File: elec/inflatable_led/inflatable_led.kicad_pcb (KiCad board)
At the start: 2 copper layers, 100.1 x 100 mm, 87 parts, among them J1 Header-Male-2.54_1x20, J2 Conn_01x02_Pin, J3 Conn_01x02_Pin, SW1 TS-1093C-A7B2-D1, U1 RP2040, U2 W25Q128JVSIQTR, U3 TPS61165DRVR, U4 BQ24040DSQR, U5 AMS1117-3.3, U6 F.0603.00026/P2-0603B1TS2-06T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, U7 SI2323DS, X1 X322512MSB4SI

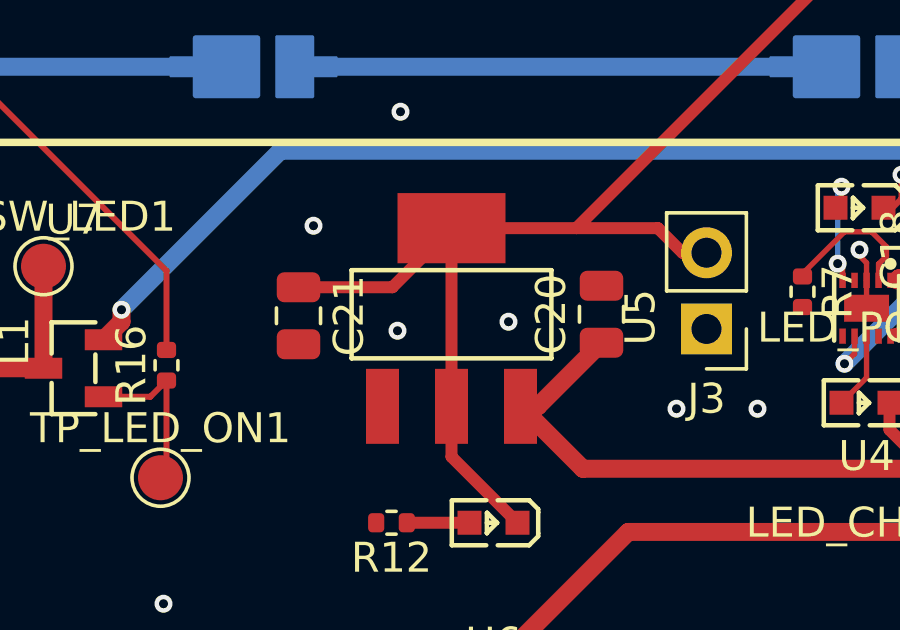
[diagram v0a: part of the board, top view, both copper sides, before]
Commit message: fix footprint + add pn
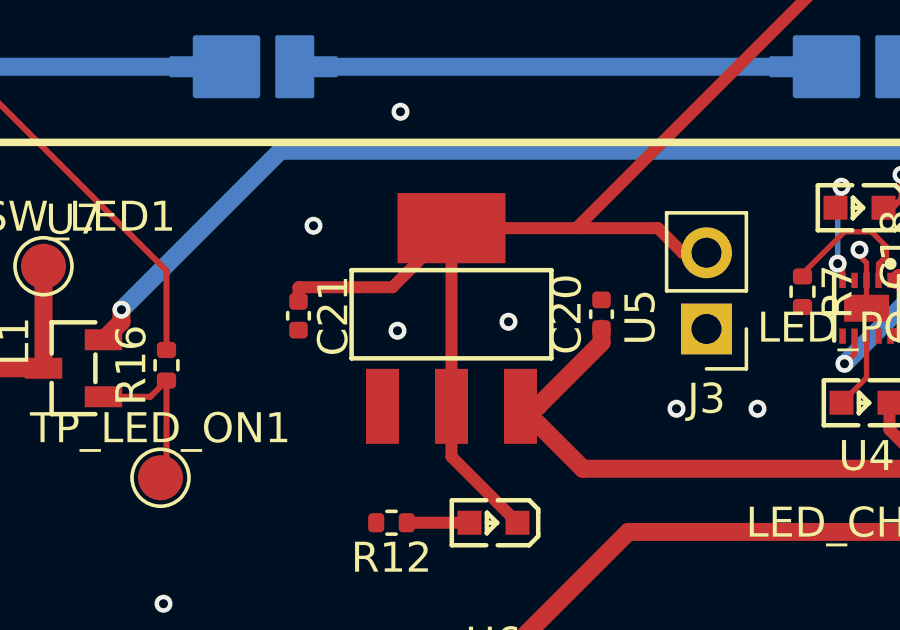
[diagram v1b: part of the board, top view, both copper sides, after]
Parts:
- C20, C21: footprint Capacitor_SMD:C_0805_2012Metric -> Capacitor_SMD:C_0402_1005Metric
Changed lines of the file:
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@@
 		)
 	)
-	(footprint "Capacitor_SMD:C_0805_2012Metric"
+	(footprint "Capacitor_SMD:C_0402_1005Metric"
 		(layer "F.Cu")
 		(at 111.6 128.25 90)
-		(descr "Capacitor SMD 0805 (2012 Metric), square (rectangular) end terminal, IPC_7351 nominal, (Body size source: IPC-SM-782 page 76, https://www.pcb-3d.com/wordpress/wp-content/uploads/ipc-sm-782a_amendment_1_and_2.pdf, https://docs.google.com/spreadsheets/d/1BsfQQcO9C6DZCsRaXUlFlo91Tg2WpOkGARC1WS5S8t0/edit?usp=sharing), generated with kicad-footprint-generator")
+		(descr "Capacitor SMD 0402 (1005 Metric), square (rectangular) end terminal, IPC_7351 nominal, (Body size source: IPC-SM-782 page 76, https://www.pcb-3d.com/wordpress/wp-content/uploads/ipc-sm-782a_amendment_1_and_2.pdf), generated with kicad-footprint-generator")
 		(tags "capacitor")
 		(property "Reference" "C20"
-			(at 0 -1.68 -90)
+			(at 0 -1.16 90)
 			(layer "F.SilkS")
 			(effects
@@
 		)
 		(property "Value" "100nF"
-			(at 0 1.68 -90)
+			(at 0 1.16 90)
 			(layer "F.Fab")
 			(effects
@@
 			)
 		)
-		(property "Footprint" "Capacitor_SMD:C_0805_2012Metric"
+		(property "Footprint" "Capacitor_SMD:C_0402_1005Metric"
 			(at 0 0 90)
 			(unlocked yes)
@@
 		(attr smd)
 		(fp_line
-			(start -0.261252 -0.735)
-			(end 0.261252 -0.735)
+			(start -0.107836 -0.36)
+			(end 0.107836 -0.36)
 			(stroke
 				(width 0.12)
@@
 		)
 		(fp_line
-			(start -0.261252 0.735)
-			(end 0.261252 0.735)
+			(start -0.107836 0.36)
+			(end 0.107836 0.36)
 			(stroke
 				(width 0.12)
@@
 		)
 		(fp_line
-			(start 1.7 -0.98)
-			(end 1.7 0.98)
+			(start 0.91 -0.46)
+			(end 0.91 0.46)
 			(stroke
 				(width 0.05)
@@
 		)
 		(fp_line
-			(start -1.7 -0.98)
-			(end 1.7 -0.98)
+			(start -0.91 -0.46)
+			(end 0.91 -0.46)
 			(stroke
 				(width 0.05)
@@
 		)
 		(fp_line
-			(start 1.7 0.98)
-			(end -1.7 0.98)
+			(start 0.91 0.46)
+			(end -0.91 0.46)
 			(stroke
 				(width 0.05)
@@
 		)
 		(fp_line
-			(start -1.7 0.98)
-			(end -1.7 -0.98)
+			(start -0.91 0.46)
+			(end -0.91 -0.46)
 			(stroke
 				(width 0.05)
@@
 		)
 		(fp_line
-			(start 1 -0.625)
-			(end 1 0.625)
+			(start 0.5 -0.25)
+			(end 0.5 0.25)
 			(stroke
 				(width 0.1)
@@
 		)
 		(fp_line
-			(start -1 -0.625)
-			(end 1 -0.625)
+			(start -0.5 -0.25)
+			(end 0.5 -0.25)
 			(stroke
 				(width 0.1)
@@
 		)
 		(fp_line
-			(start 1 0.625)
-			(end -1 0.625)
+			(start 0.5 0.25)
+			(end -0.5 0.25)
 			(stroke
 				(width 0.1)
@@
 		)
 		(fp_line
-			(start -1 0.625)
-			(end -1 -0.625)
+			(start -0.5 0.25)
+			(end -0.5 -0.25)
 			(stroke
 				(width 0.1)
@@
 		)
 		(fp_text user "${REFERENCE}"
-			(at 0 0 -90)
+			(at 0 0 90)
 			(layer "F.Fab")
 			(effects
 				(font
-					(size 0.5 0.5)
-					(thickness 0.08)
+					(size 0.25 0.25)
+					(thickness 0.04)
 				)
 			)
 		)
 		(pad "1" smd roundrect
-			(at -0.95 0 90)
-			(size 1 1.45)
+			(at -0.48 0 90)
+			(size 0.56 0.62)
 			(layers "F.Cu" "F.Paste" "F.Mask")
 			(roundrect_rratio 0.25)
@@
 		)
 		(pad "2" smd roundrect
-			(at 0.95 0 90)
-			(size 1 1.45)
+			(at 0.48 0 90)
+			(size 0.56 0.62)
 			(layers "F.Cu" "F.Paste" "F.Mask")
 			(roundrect_rratio 0.25)
@@
 			(pintype "passive")
 		)
-		(model "${KICAD8_3DMODEL_DIR}/Capacitor_SMD.3dshapes/C_0805_2012Metric.wrl"
+		(model "${KICAD8_3DMODEL_DIR}/Capacitor_SMD.3dshapes/C_0402_1005Metric.wrl"
 			(offset
 				(xyz 0 0 0)
@@
 		)
 	)
-	(footprint "Capacitor_SMD:C_0805_2012Metric"
+	(footprint "Capacitor_SMD:C_0402_1005Metric"
 		(layer "F.Cu")
 		(at 101.5 128.3 -90)
-		(descr "Capacitor SMD 0805 (2012 Metric), square (rectangular) end terminal, IPC_7351 nominal, (Body size source: IPC-SM-782 page 76, https://www.pcb-3d.com/wordpress/wp-content/uploads/ipc-sm-782a_amendment_1_and_2.pdf, https://docs.google.com/spreadsheets/d/1BsfQQcO9C6DZCsRaXUlFlo91Tg2WpOkGARC1WS5S8t0/edit?usp=sharing), generated with kicad-footprint-generator")
+		(descr "Capacitor SMD 0402 (1005 Metric), square (rectangular) end terminal, IPC_7351 nominal, (Body size source: IPC-SM-782 page 76, https://www.pcb-3d.com/wordpress/wp-content/uploads/ipc-sm-782a_amendment_1_and_2.pdf), generated with kicad-footprint-generator")
 		(tags "capacitor")
 		(property "Reference" "C21"
-			(at 0 -1.68 90)
+			(at 0 -1.16 -90)
 			(layer "F.SilkS")
 			(effects
@@
 		)
 		(property "Value" "100nF"
-			(at 0 1.68 90)
+			(at 0 1.16 -90)
 			(layer "F.Fab")
 			(effects
@@
 			)
 		)
-		(property "Footprint" "Capacitor_SMD:C_0805_2012Metric"
+		(property "Footprint" "Capacitor_SMD:C_0402_1005Metric"
 			(at 0 0 -90)
 			(unlocked yes)
@@
 		(attr smd)
 		(fp_line
-			(start -0.261252 0.735)
-			(end 0.261252 0.735)
+			(start -0.107836 0.36)
+			(end 0.107836 0.36)
 			(stroke
 				(width 0.12)
@@
 		)
 		(fp_line
-			(start -0.261252 -0.735)
-			(end 0.261252 -0.735)
+			(start -0.107836 -0.36)
+			(end 0.107836 -0.36)
 			(stroke
 				(width 0.12)
@@
 		)
 		(fp_line
-			(start -1.7 0.98)
-			(end -1.7 -0.98)
+			(start -0.91 0.46)
+			(end -0.91 -0.46)
 			(stroke
 				(width 0.05)
@@
 		)
 		(fp_line
-			(start 1.7 0.98)
-			(end -1.7 0.98)
+			(start 0.91 0.46)
+			(end -0.91 0.46)
 			(stroke
 				(width 0.05)
@@
 		)
 		(fp_line
-			(start -1.7 -0.98)
-			(end 1.7 -0.98)
+			(start -0.91 -0.46)
+			(end 0.91 -0.46)
 			(stroke
 				(width 0.05)
@@
 		)
 		(fp_line
-			(start 1.7 -0.98)
-			(end 1.7 0.98)
+			(start 0.91 -0.46)
+			(end 0.91 0.46)
 			(stroke
 				(width 0.05)
@@
 		)
 		(fp_line
-			(start -1 0.625)
-			(end -1 -0.625)
+			(start -0.5 0.25)
+			(end -0.5 -0.25)
 			(stroke
 				(width 0.1)
@@
 		)
 		(fp_line
-			(start 1 0.625)
-			(end -1 0.625)
+			(start 0.5 0.25)
+			(end -0.5 0.25)
 			(stroke
 				(width 0.1)
@@
 		)
 		(fp_line
-			(start -1 -0.625)
-			(end 1 -0.625)
+			(start -0.5 -0.25)
+			(end 0.5 -0.25)
 			(stroke
 				(width 0.1)
@@
 		)
 		(fp_line
-			(start 1 -0.625)
-			(end 1 0.625)
+			(start 0.5 -0.25)
+			(end 0.5 0.25)
 			(stroke
 				(width 0.1)
@@
 		)
 		(fp_text user "${REFERENCE}"
-			(at 0 0 90)
+			(at 0 0 -90)
 			(layer "F.Fab")
 			(effects
 				(font
-					(size 0.5 0.5)
-					(thickness 0.08)
+					(size 0.25 0.25)
+					(thickness 0.04)
 				)
 			)
 		)
 		(pad "1" smd roundrect
-			(at -0.95 0 270)
-			(size 1 1.45)
+			(at -0.48 0 270)
+			(size 0.56 0.62)
 			(layers "F.Cu" "F.Paste" "F.Mask")
 			(roundrect_rratio 0.25)
@@
 		)
 		(pad "2" smd roundrect
-			(at 0.95 0 270)
-			(size 1 1.45)
+			(at 0.48 0 270)
+			(size 0.56 0.62)
 			(layers "F.Cu" "F.Paste" "F.Mask")
 			(roundrect_rratio 0.25)
@@
 			(pintype "passive")
 		)
-		(model "${KICAD8_3DMODEL_DIR}/Capacitor_SMD.3dshapes/C_0805_2012Metric.wrl"
+		(model "${KICAD8_3DMODEL_DIR}/Capacitor_SMD.3dshapes/C_0402_1005Metric.wrl"
 			(offset
 				(xyz 0 0 0)
@@
 	)
 	(segment
+		(start 101.5 127.35)
+		(end 101.5 127.82)
+		(width 0.4)
+		(layer "F.Cu")
+		(net 3)
+	)
+	(segment
 		(start 131.1 105.039848)
 		(end 131.1 96.15)
@@
 		(width 0.6)
 		(layer "F.Cu")
+		(net 53)
+	)
+	(segment
+		(start 111.6 129.2)
+		(end 111.6 128.73)
+		(width 0.6)
+		(layer "F.Cu")

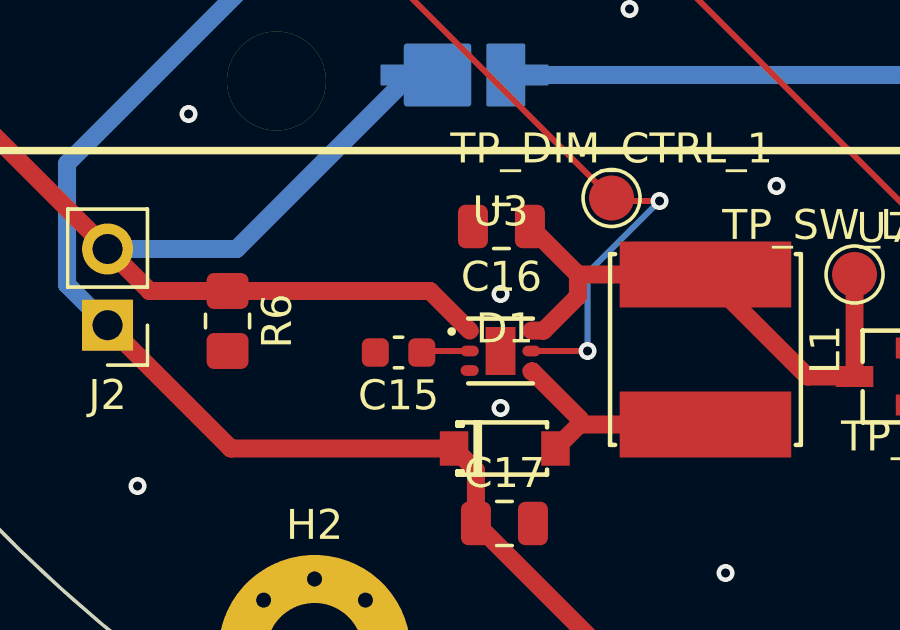
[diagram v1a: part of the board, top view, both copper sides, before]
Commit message: fix more footprints
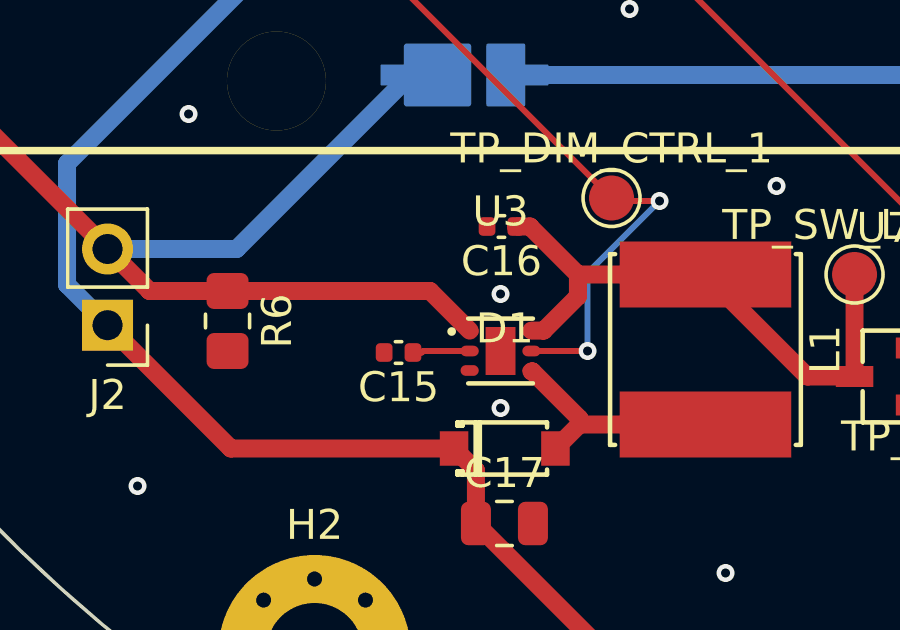
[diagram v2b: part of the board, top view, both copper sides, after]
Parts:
- C15: footprint Capacitor_SMD:C_0603_1608Metric -> Capacitor_SMD:C_0402_1005Metric
- C16: footprint Capacitor_SMD:C_0805_2012Metric -> Capacitor_SMD:C_0402_1005Metric
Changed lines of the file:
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@@
 			)
 		)
-		(property "LCSC Part" "C49678"
+		(property "LCSC Part" "C1525"
 			(at 0 0 -90)
 			(unlocked yes)
@@
 		)
 	)
-	(footprint "Capacitor_SMD:C_0603_1608Metric"
+	(footprint "Capacitor_SMD:C_0402_1005Metric"
 		(layer "F.Cu")
 		(at 77.8 129.25 180)
-		(descr "Capacitor SMD 0603 (1608 Metric), square (rectangular) end terminal, IPC_7351 nominal, (Body size source: IPC-SM-782 page 76, https://www.pcb-3d.com/wordpress/wp-content/uploads/ipc-sm-782a_amendment_1_and_2.pdf), generated with kicad-footprint-generator")
+		(descr "Capacitor SMD 0402 (1005 Metric), square (rectangular) end terminal, IPC_7351 nominal, (Body size source: IPC-SM-782 page 76, https://www.pcb-3d.com/wordpress/wp-content/uploads/ipc-sm-782a_amendment_1_and_2.pdf), generated with kicad-footprint-generator")
 		(tags "capacitor")
 		(property "Reference" "C15"
-			(at 0 -1.43 180)
+			(at 0 -1.16 180)
 			(layer "F.SilkS")
 			(effects
@@
 		)
 		(property "Value" "220nF"
-			(at 0 1.43 180)
+			(at 0 1.16 180)
 			(layer "F.Fab")
 			(effects
@@
 			)
 		)
-		(property "Footprint" "Capacitor_SMD:C_0603_1608Metric"
+		(property "Footprint" "Capacitor_SMD:C_0402_1005Metric"
 			(at 0 0 180)
 			(unlocked yes)
@@
 		(attr smd)
 		(fp_line
-			(start -0.14058 0.51)
-			(end 0.14058 0.51)
+			(start -0.107836 0.36)
+			(end 0.107836 0.36)
 			(stroke
 				(width 0.12)
@@
 		)
 		(fp_line
-			(start -0.14058 -0.51)
-			(end 0.14058 -0.51)
+			(start -0.107836 -0.36)
+			(end 0.107836 -0.36)
 			(stroke
 				(width 0.12)
@@
 		)
 		(fp_line
-			(start 1.48 0.73)
-			(end -1.48 0.73)
+			(start 0.91 0.46)
+			(end -0.91 0.46)
 			(stroke
 				(width 0.05)
@@
 		)
 		(fp_line
-			(start 1.48 -0.73)
-			(end 1.48 0.73)
+			(start 0.91 -0.46)
+			(end 0.91 0.46)
 			(stroke
 				(width 0.05)
@@
 		)
 		(fp_line
-			(start -1.48 0.73)
-			(end -1.48 -0.73)
+			(start -0.91 0.46)
+			(end -0.91 -0.46)
 			(stroke
 				(width 0.05)
@@
 		)
 		(fp_line
-			(start -1.48 -0.73)
-			(end 1.48 -0.73)
+			(start -0.91 -0.46)
+			(end 0.91 -0.46)
 			(stroke
 				(width 0.05)
@@
 		)
 		(fp_line
-			(start 0.8 0.4)
-			(end -0.8 0.4)
+			(start 0.5 0.25)
+			(end -0.5 0.25)
 			(stroke
 				(width 0.1)
@@
 		)
 		(fp_line
-			(start 0.8 -0.4)
-			(end 0.8 0.4)
+			(start 0.5 -0.25)
+			(end 0.5 0.25)
 			(stroke
 				(width 0.1)
@@
 		)
 		(fp_line
-			(start -0.8 0.4)
-			(end -0.8 -0.4)
+			(start -0.5 0.25)
+			(end -0.5 -0.25)
 			(stroke
 				(width 0.1)
@@
 		)
 		(fp_line
-			(start -0.8 -0.4)
-			(end 0.8 -0.4)
+			(start -0.5 -0.25)
+			(end 0.5 -0.25)
 			(stroke
 				(width 0.1)
@@
 			(effects
 				(font
-					(size 0.4 0.4)
-					(thickness 0.06)
+					(size 0.25 0.25)
+					(thickness 0.04)
 				)
 			)
 		)
 		(pad "1" smd roundrect
-			(at -0.775 0 180)
-			(size 0.9 0.95)
+			(at -0.48 0 180)
+			(size 0.56 0.62)
 			(layers "F.Cu" "F.Paste" "F.Mask")
 			(roundrect_rratio 0.25)
@@
 		)
 		(pad "2" smd roundrect
-			(at 0.775 0 180)
-			(size 0.9 0.95)
+			(at 0.48 0 180)
+			(size 0.56 0.62)
 			(layers "F.Cu" "F.Paste" "F.Mask")
 			(roundrect_rratio 0.25)
@@
 			(pintype "passive")
 		)
-		(model "${KICAD8_3DMODEL_DIR}/Capacitor_SMD.3dshapes/C_0603_1608Metric.wrl"
+		(model "${KICAD8_3DMODEL_DIR}/Capacitor_SMD.3dshapes/C_0402_1005Metric.wrl"
 			(offset
 				(xyz 0 0 0)
@@
 			)
 		)
-		(property "LCSC Part" "C49678"
+		(property "LCSC Part" "C1525"
 			(at 0 0 180)
 			(unlocked yes)
@@
 		)
 	)
-	(footprint "Capacitor_SMD:C_0805_2012Metric"
+	(footprint "Capacitor_SMD:C_0402_1005Metric"
 		(layer "F.Cu")
 		(at 81.23 125.05 180)
-		(descr "Capacitor SMD 0805 (2012 Metric), square (rectangular) end terminal, IPC_7351 nominal, (Body size source: IPC-SM-782 page 76, https://www.pcb-3d.com/wordpress/wp-content/uploads/ipc-sm-782a_amendment_1_and_2.pdf, https://docs.google.com/spreadsheets/d/1BsfQQcO9C6DZCsRaXUlFlo91Tg2WpOkGARC1WS5S8t0/edit?usp=sharing), generated with kicad-footprint-generator")
+		(descr "Capacitor SMD 0402 (1005 Metric), square (rectangular) end terminal, IPC_7351 nominal, (Body size source: IPC-SM-782 page 76, https://www.pcb-3d.com/wordpress/wp-content/uploads/ipc-sm-782a_amendment_1_and_2.pdf), generated with kicad-footprint-generator")
 		(tags "capacitor")
 		(property "Reference" "C16"
-			(at 0 -1.68 180)
+			(at 0 -1.16 180)
 			(layer "F.SilkS")
 			(effects
@@
 		)
 		(property "Value" "4.7uF"
-			(at 0 1.68 180)
+			(at 0 1.16 180)
 			(layer "F.Fab")
 			(effects
@@
 			)
 		)
-		(property "Footprint" "Capacitor_SMD:C_0805_2012Metric"
+		(property "Footprint" "Capacitor_SMD:C_0402_1005Metric"
 			(at 0 0 180)
 			(unlocked yes)
@@
 		(attr smd)
 		(fp_line
-			(start -0.261252 0.735)
-			(end 0.261252 0.735)
+			(start -0.107836 0.36)
+			(end 0.107836 0.36)
 			(stroke
 				(width 0.12)
@@
 		)
 		(fp_line
-			(start -0.261252 -0.735)
-			(end 0.261252 -0.735)
+			(start -0.107836 -0.36)
+			(end 0.107836 -0.36)
 			(stroke
 				(width 0.12)
@@
 		)
 		(fp_line
-			(start 1.7 0.98)
-			(end -1.7 0.98)
+			(start 0.91 0.46)
+			(end -0.91 0.46)
 			(stroke
 				(width 0.05)
@@
 		)
 		(fp_line
-			(start 1.7 -0.98)
-			(end 1.7 0.98)
+			(start 0.91 -0.46)
+			(end 0.91 0.46)
 			(stroke
 				(width 0.05)
@@
 		)
 		(fp_line
-			(start -1.7 0.98)
-			(end -1.7 -0.98)
+			(start -0.91 0.46)
+			(end -0.91 -0.46)
 			(stroke
 				(width 0.05)
@@
 		)
 		(fp_line
-			(start -1.7 -0.98)
-			(end 1.7 -0.98)
+			(start -0.91 -0.46)
+			(end 0.91 -0.46)
 			(stroke
 				(width 0.05)
@@
 		)
 		(fp_line
-			(start 1 0.625)
-			(end -1 0.625)
+			(start 0.5 0.25)
+			(end -0.5 0.25)
 			(stroke
 				(width 0.1)
@@
 		)
 		(fp_line
-			(start 1 -0.625)
-			(end 1 0.625)
+			(start 0.5 -0.25)
+			(end 0.5 0.25)
 			(stroke
 				(width 0.1)
@@
 		)
 		(fp_line
-			(start -1 0.625)
-			(end -1 -0.625)
+			(start -0.5 0.25)
+			(end -0.5 -0.25)
 			(stroke
 				(width 0.1)
@@
 		)
 		(fp_line
-			(start -1 -0.625)
-			(end 1 -0.625)
+			(start -0.5 -0.25)
+			(end 0.5 -0.25)
 			(stroke
 				(width 0.1)
@@
 			(effects
 				(font
-					(size 0.5 0.5)
-					(thickness 0.08)
+					(size 0.25 0.25)
+					(thickness 0.04)
 				)
 			)
 		)
 		(pad "1" smd roundrect
-			(at -0.95 0 180)
-			(size 1 1.45)
+			(at -0.48 0 180)
+			(size 0.56 0.62)
 			(layers "F.Cu" "F.Paste" "F.Mask")
 			(roundrect_rratio 0.25)
@@
 		)
 		(pad "2" smd roundrect
-			(at 0.95 0 180)
-			(size 1 1.45)
+			(at 0.48 0 180)
+			(size 0.56 0.62)
 			(layers "F.Cu" "F.Paste" "F.Mask")
 			(roundrect_rratio 0.25)
@@
 			(pintype "passive")
 		)
-		(model "${KICAD8_3DMODEL_DIR}/Capacitor_SMD.3dshapes/C_0805_2012Metric.wrl"
+		(model "${KICAD8_3DMODEL_DIR}/Capacitor_SMD.3dshapes/C_0402_1005Metric.wrl"
 			(offset
 				(xyz 0 0 0)
@@
 			)
 		)
-		(property "LCSC Part" "C49678"
+		(property "LCSC Part" "C1525"
 			(at 0 0 -90)
 			(unlocked yes)
@@
 			)
 		)
-		(property "LCSC Part" "C49678"
+		(property "LCSC Part" "C1525"
 			(at 0 0 0)
 			(unlocked yes)
@@
 			)
 		)
-		(property "LCSC Part" "C49678"
+		(property "LCSC Part" "C1525"
 			(at 0 0 0)
 			(unlocked yes)
@@
 			)
 		)
-		(property "LCSC Part" "C49678"
+		(property "LCSC Part" "C1525"
 			(at 0 0 0)
 			(unlocked yes)
@@
 			)
 		)
-		(property "LCSC Part" "C49678"
+		(property "LCSC Part" "C1525"
 			(at 0 0 90)
 			(unlocked yes)
@@
 			)
 		)
-		(property "LCSC Part" "C49678"
+		(property "LCSC Part" "C1525"
 			(at 0 0 180)
 			(unlocked yes)
@@
 			)
 		)
-		(property "LCSC Part" "C49678"
+		(property "LCSC Part" "C1525"
 			(at 0 0 0)
 			(unlocked yes)
@@
 			)
 		)
+		(property "LCSC Part" "C2076855"
+			(at 0 0 -90)
+			(unlocked yes)
+			(layer "F.Fab")
+			(hide yes)
+			(effects
+				(font
+					(size 1 1)
+					(thickness 0.15)
+				)
+			)
+		)
 		(property ki_fp_filters "R_*")
 		(sheetname "Root")
@@
 			)
 		)
-		(property "LCSC Part" "C49678"
+		(property "LCSC Part" "C1525"
 			(at 0 0 -90)
 			(unlocked yes)
@@
 	)
 	(segment
+		(start 82.18 125.05)
+		(end 81.71 125.05)
+		(width 0.6)
+		(layer "F.Cu")
+		(net 54)
+	)
+	(segment
 		(start 83.78 127.376665)
 		(end 82.636665 128.52)
@@
 		(width 0.2)
 		(layer "F.Cu")
+		(net 64)
+	)
+	(segment
+		(start 78.575 129.25)
+		(end 78.28 129.25)
+		(width 0.2)
+		(layer "F.Cu")

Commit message: leds in the wrong order
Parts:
- turned LED_CHG_2 to 0 degrees
- turned LED_PG_1 to 0 degrees
- turned U6 to 0 degrees

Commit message: v1 is working, add v2 requests
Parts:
- removed C14: 10nF, Capacitor_SMD:C_0402_1005Metric
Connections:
- U2 pad 8: +3V3 -> +3.3V
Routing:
- net /QSPI_SS: track 29.1 -> 27.6 mm
